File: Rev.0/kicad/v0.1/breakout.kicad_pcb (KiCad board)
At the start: 2 copper layers, 63.5 x 77.2 mm, 40 parts, among them J1 Conn_02x10_Odd_Even, J10 Conn_02x10_Odd_Even, J12 Conn_02x10_Odd_Even, J2 Conn_02x10_Odd_Even, J3 Conn_01x02, J4 Conn_01x03_Pin, J5 Conn_01x05_Pin, M1 MountingHole_3.5mm_Pad_TopBot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, M2 MountingHole_3.5mm_Pad_TopBot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, U1 RP2040-TINY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

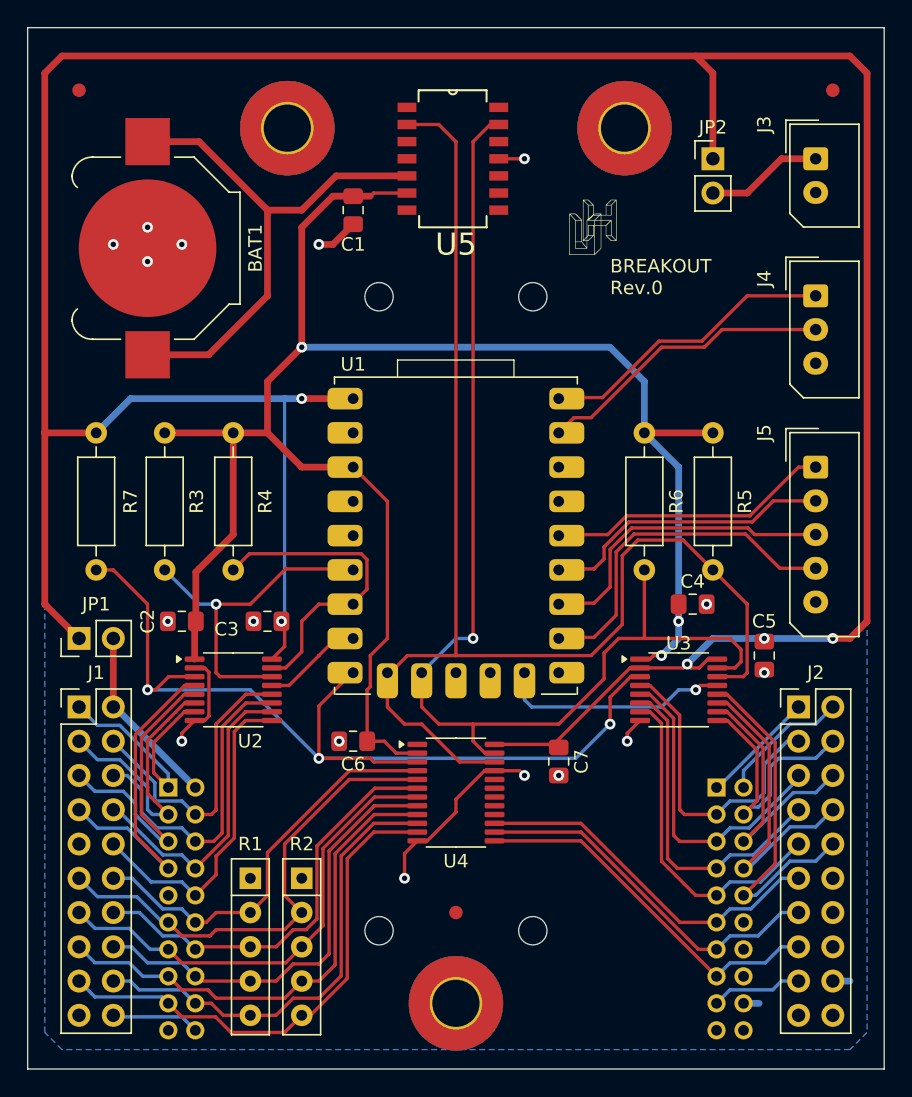
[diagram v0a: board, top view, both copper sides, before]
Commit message: Rev 0.1 added backup battery Schottky diodes
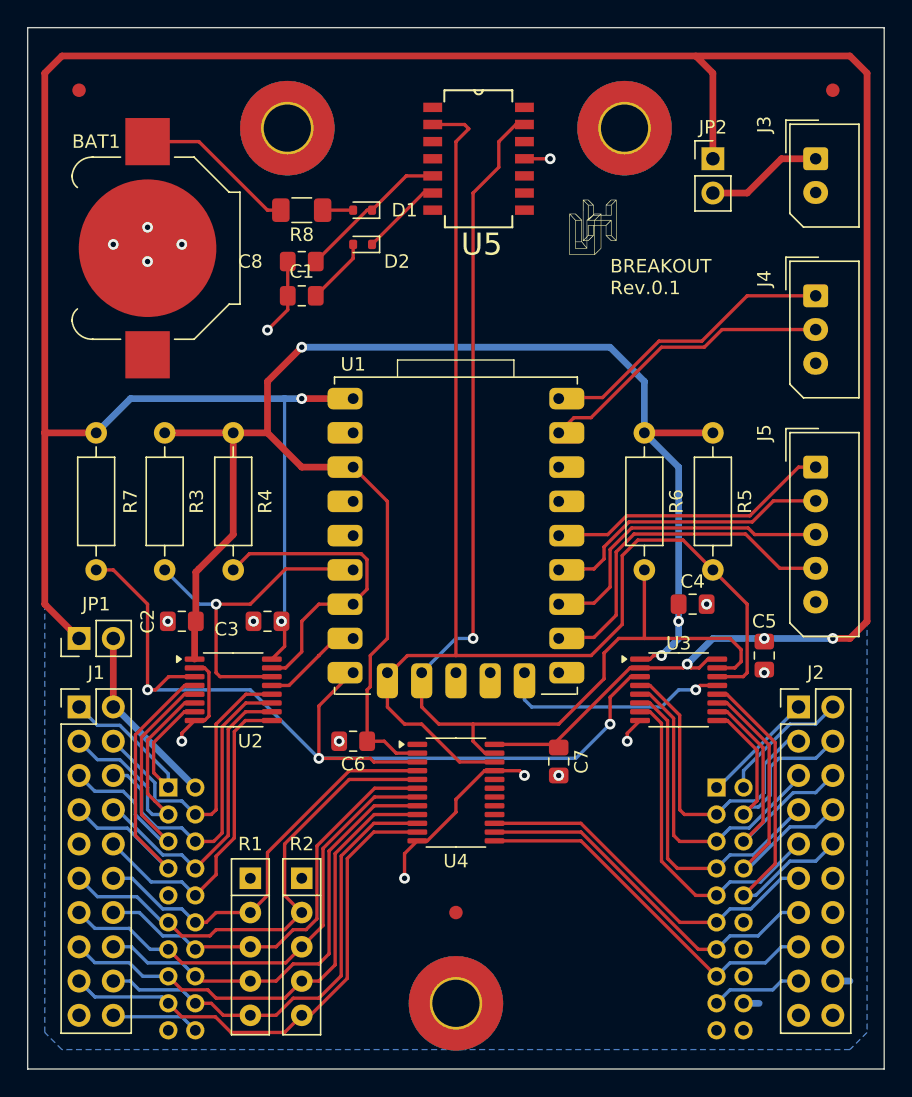
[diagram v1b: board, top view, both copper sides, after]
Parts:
- removed H1, H2, H3, H4: MountingHole_2.1mm, MountingHole:MountingHole_2.1mm
- added C8: 0.1uF, Capacitor_SMD:C_0805_2012Metric_Pad1.18x1.45mm_HandSolder, F.Cu at (95.3, 116.1)
- added D1: SDM03U40, Diode_SMD:D_SOD-523, F.Cu at (99.8, 112.3)
- added D2: SDM03U40, Diode_SMD:D_SOD-523, F.Cu at (99.8, 114.9)
- added R8: 88, Resistor_SMD:R_1206_3216Metric_Pad1.30x1.75mm_HandSolder, F.Cu at (95.3, 112.3)
- moved C1 7.41 mm to (95.3, 118.7), turned to 180 degrees
- moved U5 1.91 mm to (108.4, 108.5)
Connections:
- U5 pad 5: Net-(BAT1-+) -> Net-(D1-K)
- U5 pad 6: +3V3 -> Net-(D2-K)
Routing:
- net Net-(BAT1-+): track 39.3 -> 12.0 mm
- net +3V3: track 140.4 -> 127.8 mm
- net Net-(D1-K): track 0.00 -> 11.3 mm
- net Net-(D2-K): track 0.00 -> 6.08 mm
- net GND: track 30.8 -> 33.3 mm
- net Net-(D1-A): track 0.00 -> 2.26 mm
- net /SDA1: track 86.3 -> 87.1 mm
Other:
- board text added: "BREAKOUT Rev.0.1"
- board text removed: "BREAKOUT Rev.0"

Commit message: Rev 0.1: shuffled decoupling capacitors to correct side of Schottky diodes
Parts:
- moved C8 7.18 mm to (100.4, 111.1), turned to -90 degrees
- moved C1 5.68 mm to (100.4, 116.1), turned to -90 degrees
- moved D2 3.21 mm to (97.9, 117.4), turned to -90 degrees
- moved R8 2.84 mm to (94.0, 114.9), turned to -90 degrees
- moved D1 2.34 mm to (97.9, 113.6), turned to -90 degrees
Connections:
- C1 pad 1: +3V3 -> Net-(D2-K)
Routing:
- net Net-(D1-K): track 11.3 -> 0.00 mm
- net Net-(BAT1-+): track 12.0 -> 3.81 mm
- net GND: track 33.3 -> 27.6 mm
- net Net-(D2-K): track 6.08 -> 0.69 mm
- net +3V3: track 127.8 -> 122.9 mm
- net Net-(D1-A): track 2.26 -> 0.00 mm

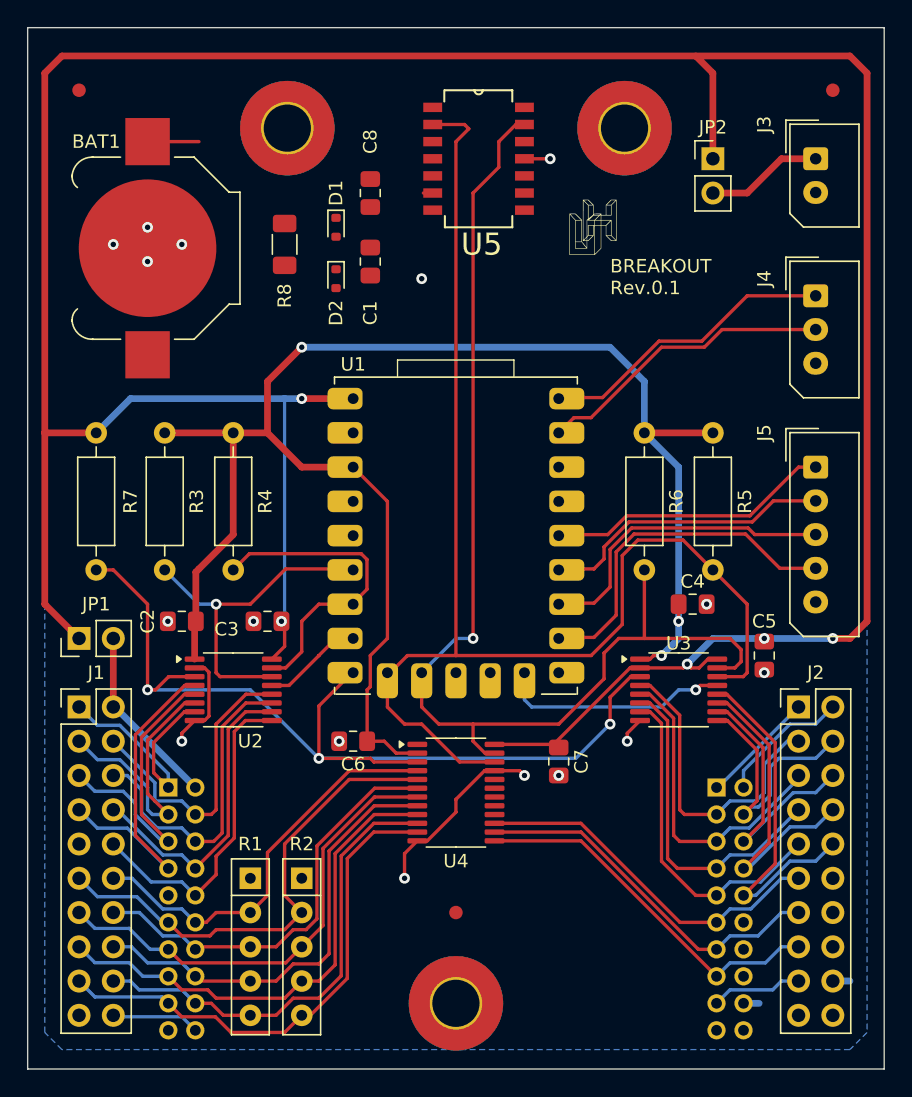
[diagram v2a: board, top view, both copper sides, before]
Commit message: Rev 0.1: added RTC battery Schottky diodes
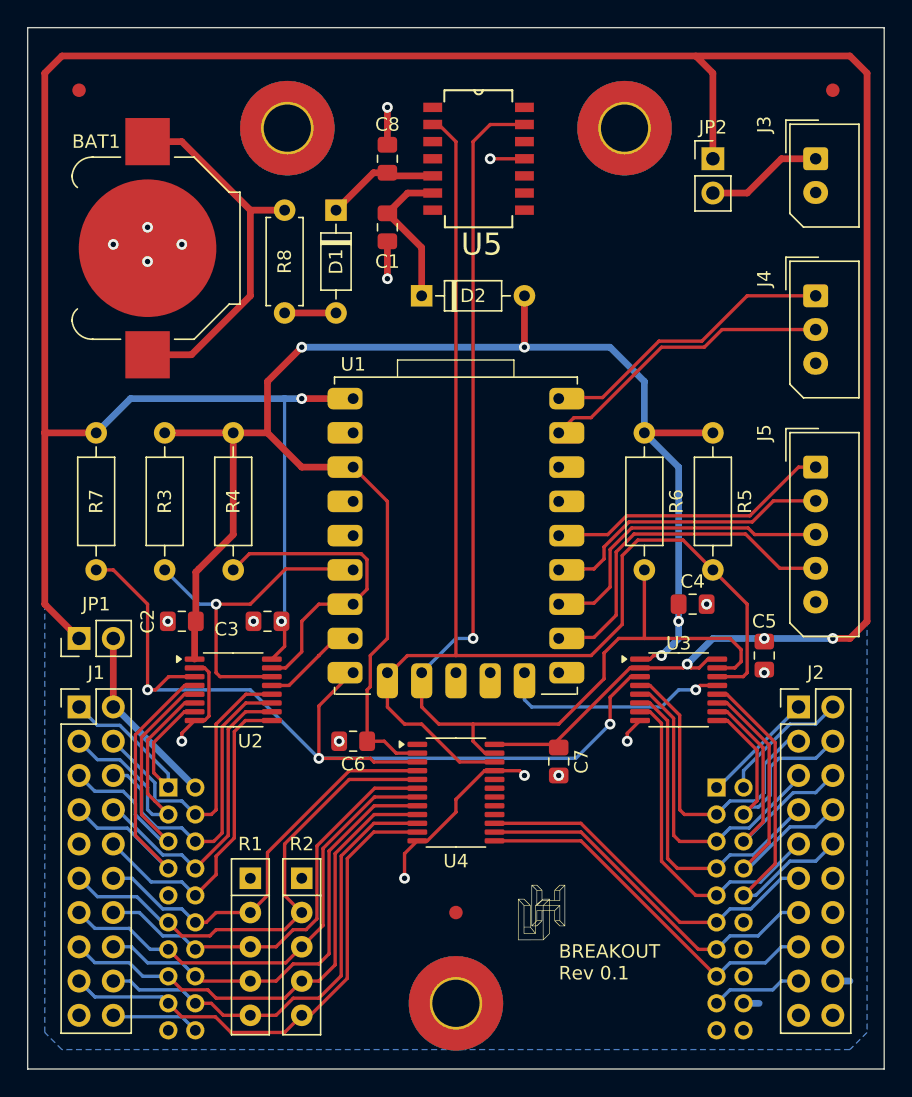
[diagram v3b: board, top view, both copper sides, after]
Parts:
- D1, D2: value SDM03U40 -> BAT43; footprint Diode_SMD:D_SOD-523 -> Diode_THT:D_DO-35_SOD27_P7.62mm_Horizontal
- R8: footprint Resistor_SMD:R_1206_3216Metric_Pad1.30x1.75mm_HandSolder -> Resistor_THT:R_Axial_DIN0207_L6.3mm_D2.5mm_P7.62mm_Horizontal
- moved G*** 50.9 mm to (113.1, 164.4)
- moved D2 6.48 mm to (104.2, 118.7), turned to 0 degrees
- moved R8 5.08 mm to (94.0, 120.0), turned to 90 degrees
- moved C1 2.84 mm to (101.7, 113.6)
- moved C8 2.84 mm to (101.7, 108.5), turned to 90 degrees
- moved D1 1.27 mm to (97.9, 112.3)
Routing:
- net Net-(BAT1-+): track 3.81 -> 28.0 mm
- net Net-(D2-K): track 0.69 -> 11.2 mm
- net Net-(D1-K): track 0.00 -> 8.41 mm
- net GND: track 27.6 -> 34.2 mm, vias 16 -> 17
- net Net-(D1-A): track 0.00 -> 3.81 mm
- net +3V3: track 122.9 -> 126.7 mm, vias 3 -> 4
- net /SCL1: track 97.6 -> 95.5 mm
- net /SDA1: track 87.1 -> 88.0 mm
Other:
- board text added: "BREAKOUT Rev 0.1"
- board text removed: "BREAKOUT Rev.0.1"
